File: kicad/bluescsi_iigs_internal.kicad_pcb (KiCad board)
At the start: 2 copper layers, 57.7 x 55.4 mm, 27 parts, among them J1 Conn_02x13_Odd_Even, J2 Conn_02x13_Odd_Even, J3 105162-0001, J4 Conn_01x02_Male, J5 Conn_01x02_Male, M1 Screw_Terminal_01x01, M2 Screw_Terminal_01x01, Q1 Q_PMOS_GSD, SW1 SW_SPDT, U1 YAAJ_BluePill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

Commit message: move d3 a bit
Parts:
- moved D3 2.29 mm to (140.7, 100.3)
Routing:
- net +5V: track 105.6 -> 103.3 mm
- net /REG_OUT: track 6.37 -> 8.66 mm
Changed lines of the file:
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@@
   )
   (module Diode_SMD:D_SOD-323_HandSoldering (layer F.Cu)
-    (at 138.43 100.33 180)
+    (at 140.716 100.33 180)
     (descr SOD-323)
     (tags SOD-323)
@@
   (segment (start 170.18 90.932) (end 168.402 92.71) (width 0.3) (layer B.Cu) (net 12))
   (segment (start 147.955 93.475) (end 151.895 93.475) (width 0.3) (layer B.Cu) (net 12))
-  (segment (start 146.815 93.98) (end 152.4 93.98) (width 0.3) (layer F.Cu) (net 12))
-  (segment (start 140.465 100.33) (end 146.815 93.98) (width 0.3) (layer F.Cu) (net 12))
-  (segment (start 139.68 100.33) (end 140.465 100.33) (width 0.3) (layer F.Cu) (net 12))
+  (segment (start 141.986 100.33) (end 148.336 93.98) (width 0.3) (layer F.Cu) (net 12))
+  (segment (start 148.336 93.98) (end 152.4 93.98) (width 0.3) (layer F.Cu) (net 12))
+  (segment (start 141.966 100.33) (end 141.986 100.33) (width 0.3) (layer F.Cu) (net 12))
   (segment (start 157.545 85.725) (end 157.545 86.995) (width 0.25) (layer B.Cu) (net 13) (status 30))
   (segment (start 157.545 60.325) (end 162.495 60.325) (width 0.25) (layer B.Cu) (net 13) (status 30))
@@
   (segment (start 178.174 85.861) (end 178.038 85.725) (width 0.25) (layer F.Cu) (net 43))
   (segment (start 184.531 85.861) (end 178.174 85.861) (width 0.25) (layer F.Cu) (net 43))
-  (segment (start 131.445 97.155) (end 130.81 97.79) (width 0.25) (layer B.Cu) (net 46))
-  (segment (start 137.18 97.155) (end 131.445 97.155) (width 0.25) (layer F.Cu) (net 46))
+  (segment (start 131.445 97.155) (end 130.81 97.79) (width 0.3) (layer B.Cu) (net 46))
+  (segment (start 137.18 97.155) (end 131.445 97.155) (width 0.3) (layer F.Cu) (net 46))
   (segment (start 133.985 95.25) (end 134.62 95.885) (width 0.3) (layer B.Cu) (net 47))
   (segment (start 130.81 95.25) (end 133.985 95.25) (width 0.3) (layer B.Cu) (net 47))
@@
   (segment (start 167.894 96.52) (end 169.037 95.377) (width 0.25) (layer B.Cu) (net 50))
   (segment (start 169.037 95.377) (end 169.037 93.472) (width 0.25) (layer B.Cu) (net 50))
-  (segment (start 130.81 100.33) (end 137.18 100.33) (width 0.3) (layer F.Cu) (net 51))
+  (segment (start 130.81 100.33) (end 139.466 100.33) (width 0.3) (layer F.Cu) (net 51))
   (segment (start 147.32 90.678) (end 147.955 90.678) (width 0.3) (layer B.Cu) (net 52))
   (segment (start 143.51 83.82) (end 144.78 82.55) (width 0.3) (layer F.Cu) (net 52))

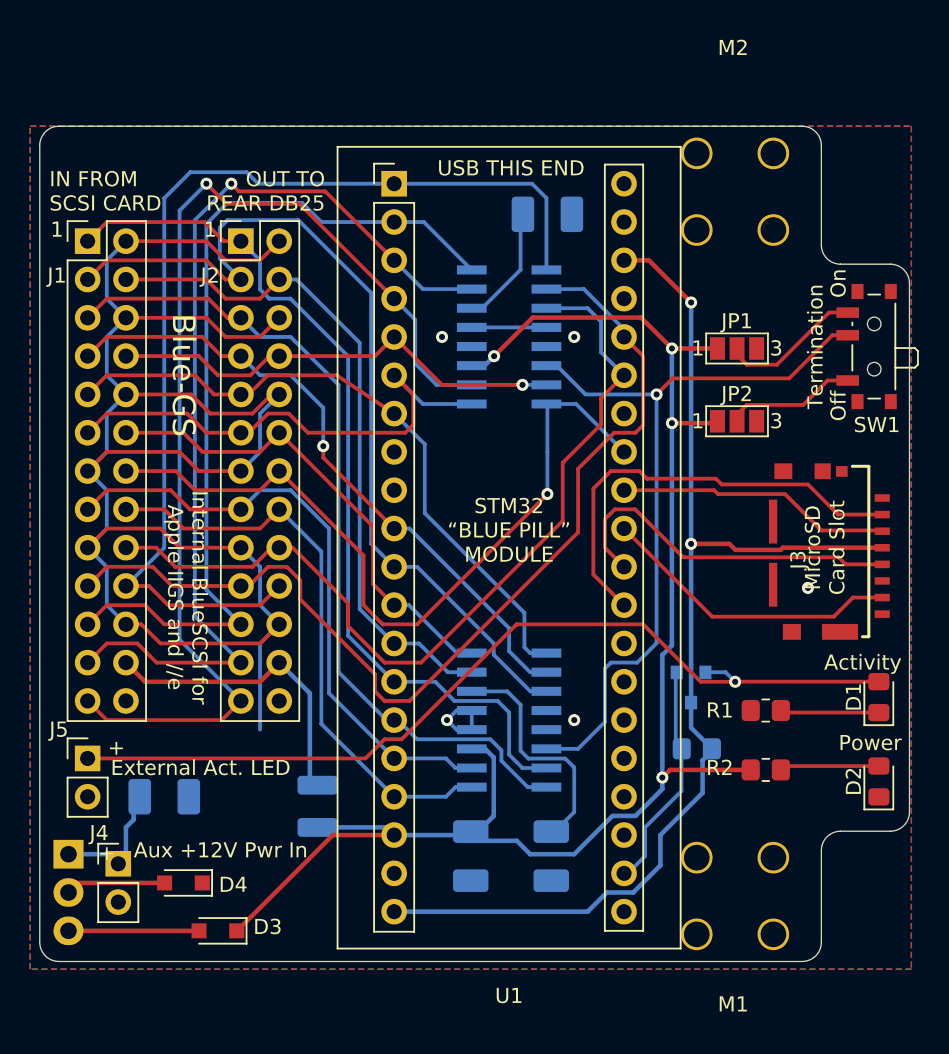
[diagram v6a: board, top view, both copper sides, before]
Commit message: replace lef mostfest with logic inverter
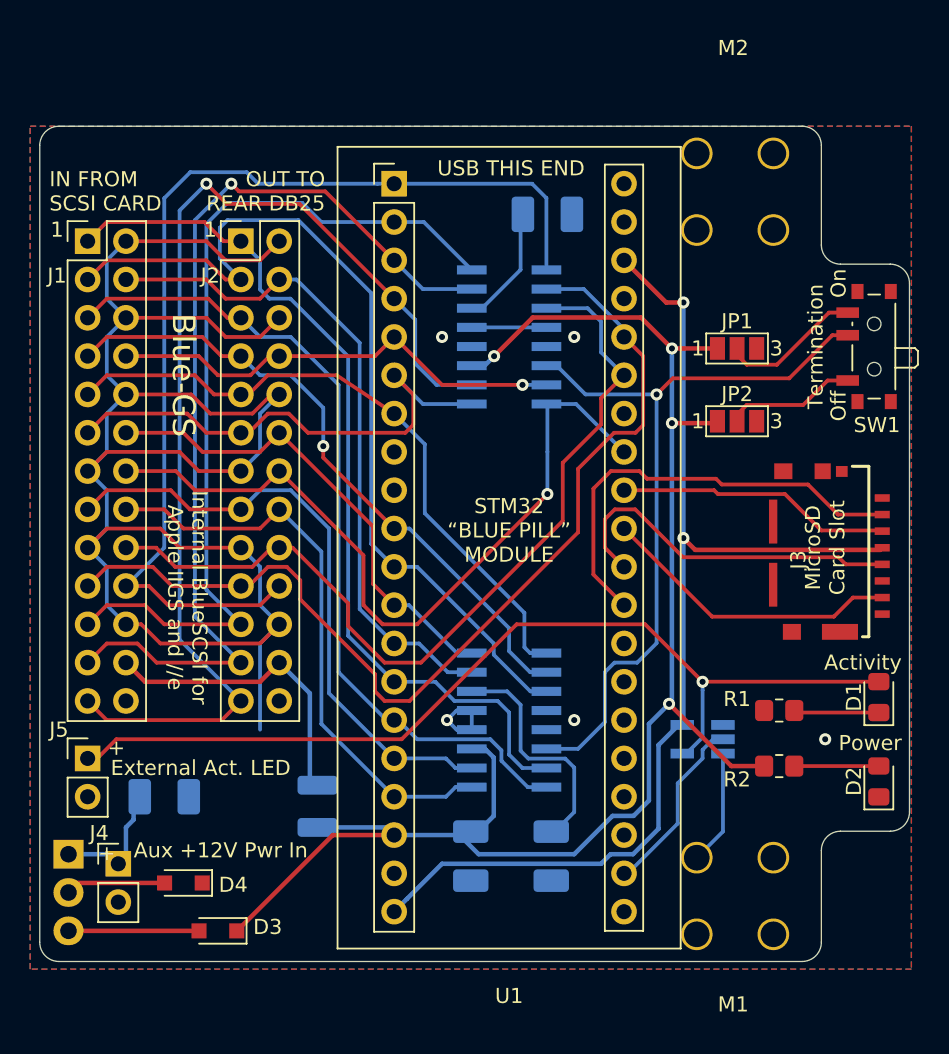
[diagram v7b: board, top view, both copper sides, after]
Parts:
- removed Q1: Q_PMOS_GSD, Package_TO_SOT_SMD:SOT-23
- removed R3: 10K, Resistor_SMD:R_0805_2012Metric_Pad1.20x1.40mm_HandSolder
- added U5: SN74LVC1G06DBVR, Package_TO_SOT_SMD:SOT-23-5_HandSoldering, B.Cu at (172.8, 87.6)
- moved R2 0.92 mm to (177.9, 89.4)
- moved R1 0.89 mm to (177.9, 85.7)
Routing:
- net GND: track 127.9 -> 135.5 mm
- net /DISK_ACT: track 15.1 -> 11.6 mm
- net Net-(D1-Pad2): track 60.1 -> 63.4 mm
- net +3V3: track 76.7 -> 74.6 mm
- net +5V: track 103.3 -> 105.2 mm
- net Net-(D1-Pad1): track 6.56 -> 5.66 mm
- net Net-(D2-Pad2): track 5.56 -> 4.94 mm

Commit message: Change regulator to back side tab up
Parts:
- U4: footprint Package_TO_SOT_THT:TO-220-3_Vertical -> Package_TO_SOT_THT:TO-220-3_Horizontal_TabUp
- moved F1 4.58 mm to (143.5, 89.5)
- moved C4 0.63 mm to (137.2, 90.8)
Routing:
- net GND: track 135.5 -> 128.0 mm
- net +5V: track 105.2 -> 112.2 mm
- net /SCSI_TERMPWR: track 21.0 -> 17.3 mm
- net /+12V_AUX: track 8.26 -> 9.27 mm
